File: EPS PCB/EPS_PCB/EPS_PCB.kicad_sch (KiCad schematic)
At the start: 0 parts

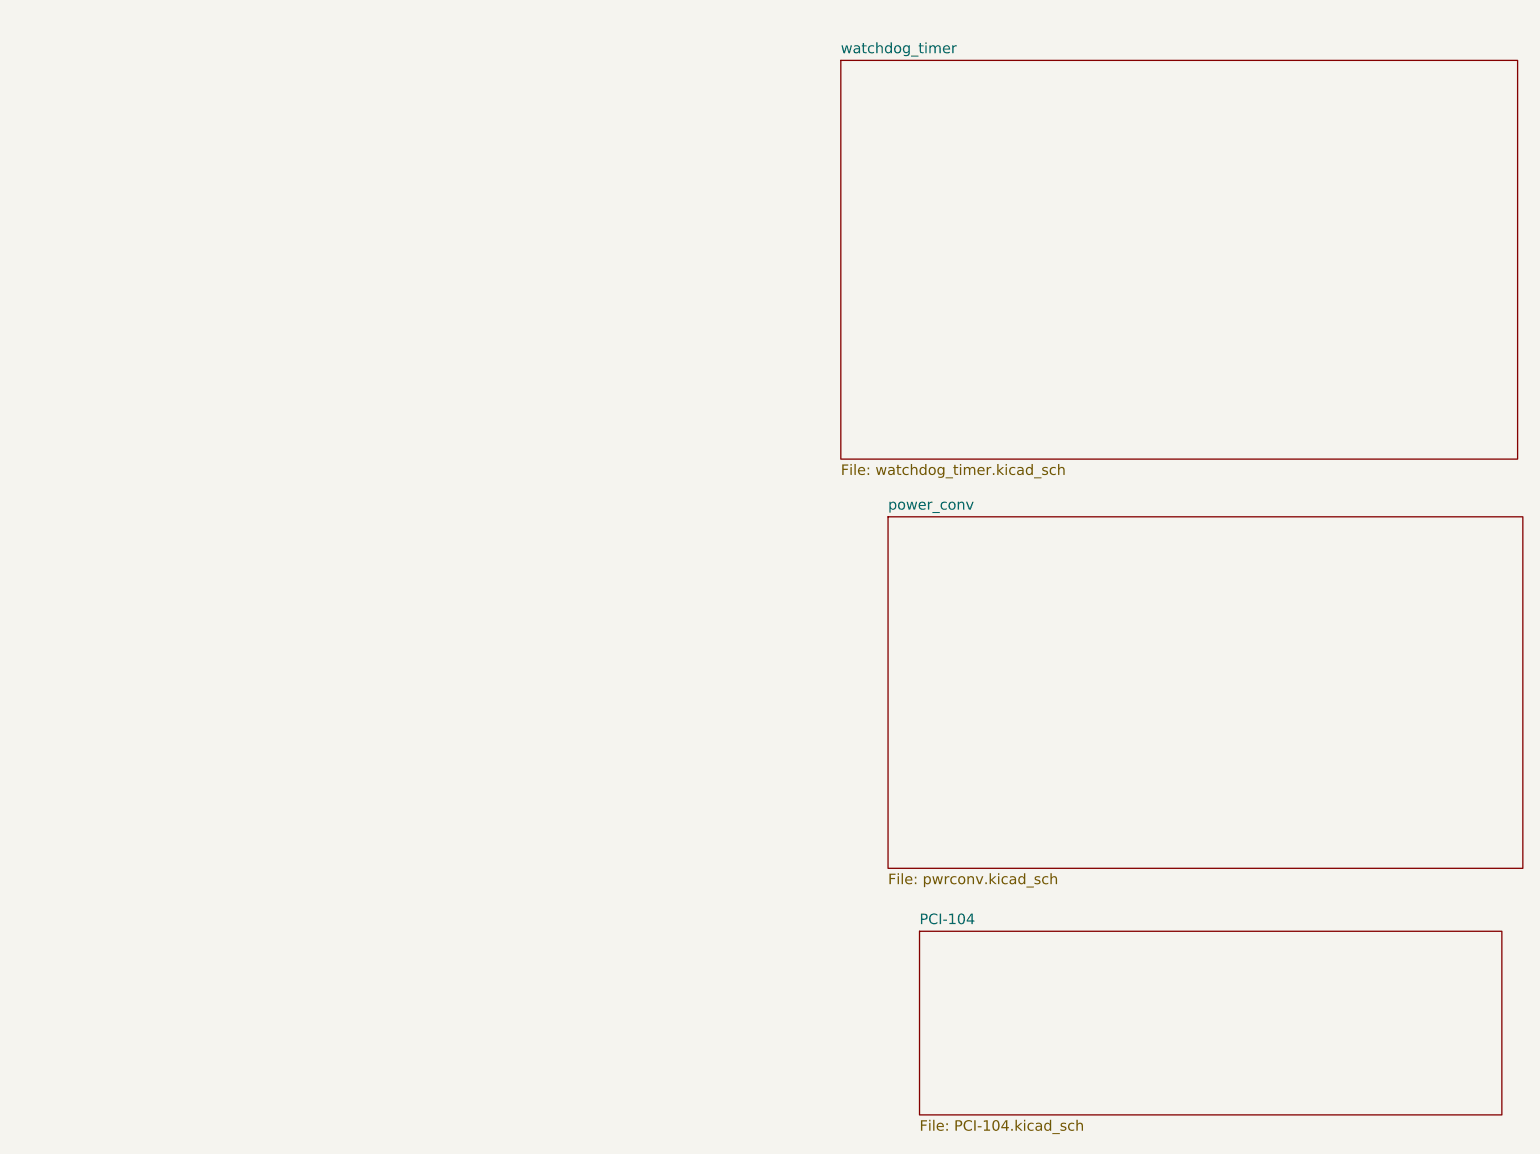
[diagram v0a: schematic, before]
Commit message: PDR Update
Added Current Measurement, Hysteresis, EFuses
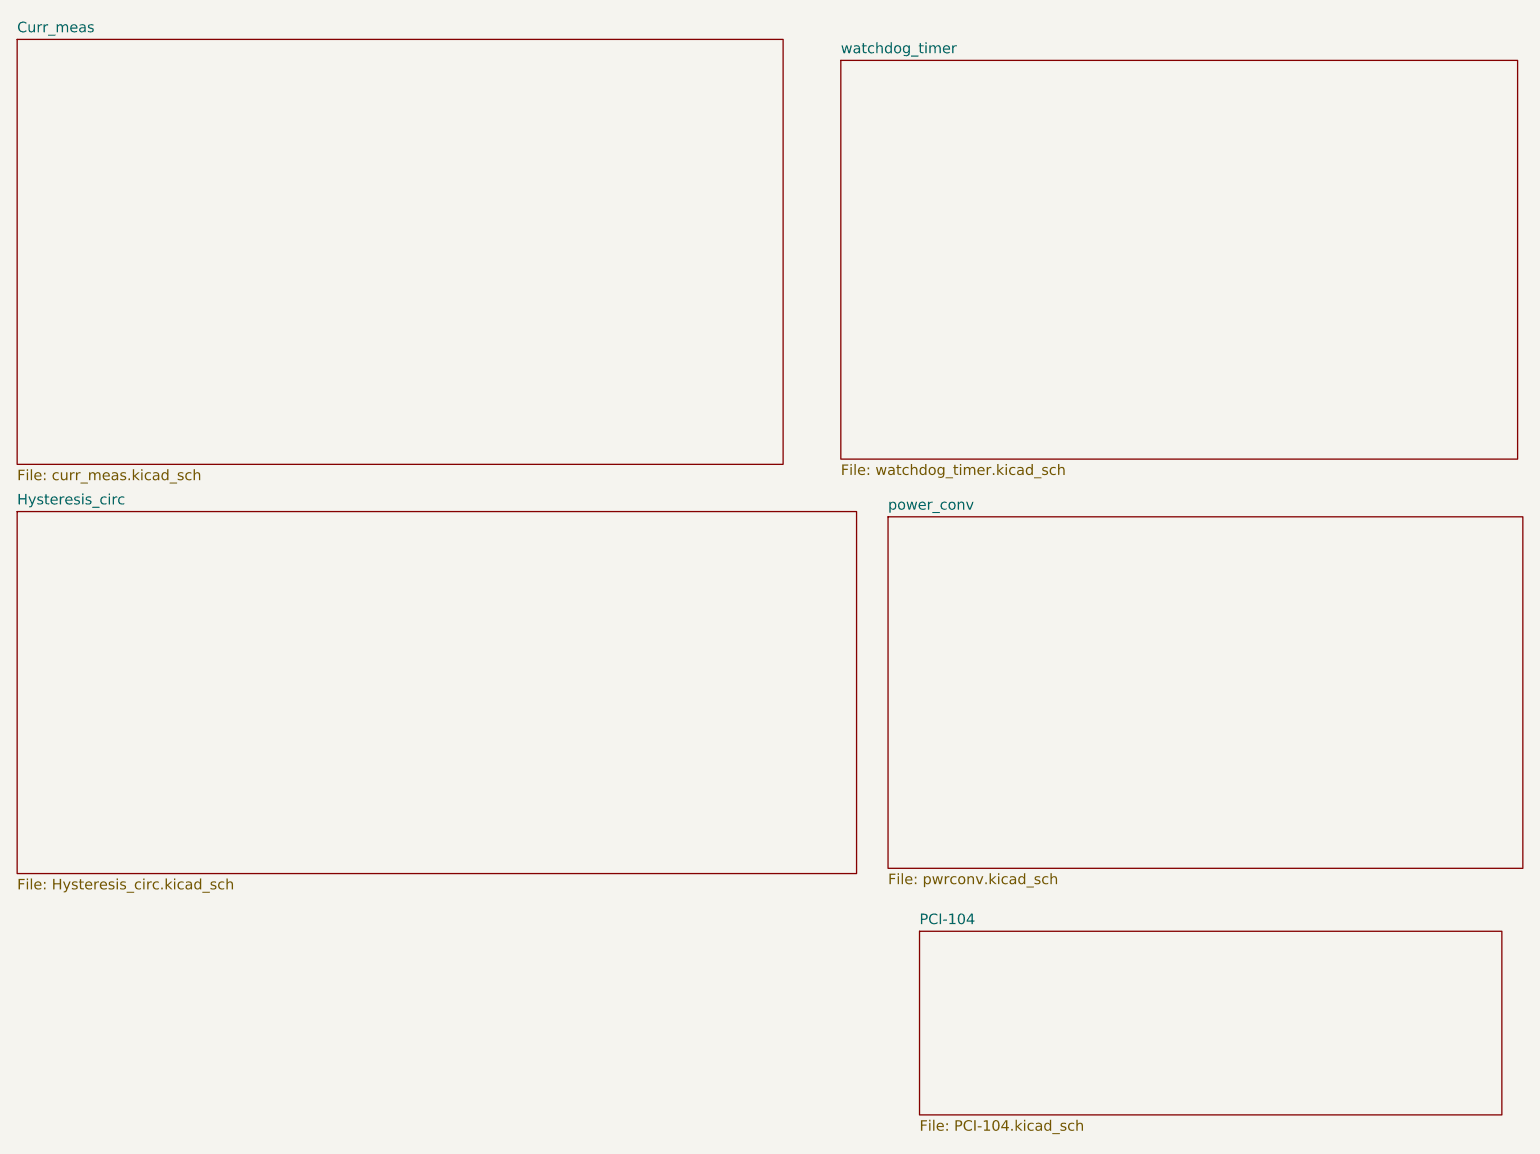
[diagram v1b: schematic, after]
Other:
- added sheet Curr_meas (curr_meas.kicad_sch)
- added sheet Hysteresis_circ (Hysteresis_circ.kicad_sch)
- company: (none) -> UW Huskysat
- title: (none) -> EPS_PDS_Circuit
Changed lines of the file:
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@@
 	(paper "A4")
 	(title_block
-		(date "2025-11-13")
+		(title "EPS_PDS_Circuit")
+		(date "2025-11-20")
+		(rev "1.0")
+		(company "UW Huskysat")
+		(comment 1 "Tracy, Maria, Phina, David, Chase")
 	)
 	(sheet
@@
 	)
 	(sheet
+		(at 90.805 27.305)
+		(size 92.71 51.435)
+		(exclude_from_sim no)
+		(in_bom yes)
+		(on_board yes)
+		(dnp no)
+		(fields_autoplaced yes)
+		(stroke
+			(width 0.1524)
+			(type solid)
+		)
+		(fill
+			(color 0 0 0 0.0000)
+		)
+		(property "Sheetname" "Curr_meas"
+			(at 90.805 26.5934 0)
+			(effects
+				(font
+					(size 1.27 1.27)
+				)
+				(justify left bottom)
+			)
+		)
+		(property "Sheetfile" "curr_meas.kicad_sch"
+			(at 90.805 79.3246 0)
+			(effects
+				(font
+					(size 1.27 1.27)
+				)
+				(justify left top)
+			)
+		)
+		(instances
+			(project "EPS_PCB"
+				(path "/e5aefcdf-1552-4881-b70a-fd78aade4bcb"
+					(page "5")
+				)
+			)
+		)
+	)
+	(sheet
 		(at 200.025 135.255)
 		(size 70.485 22.225)
@@
 				)
 			)
+		)
+	)
+	(sheet
+		(at 90.805 84.455)
+		(size 101.6 43.815)
+		(exclude_from_sim no)
+		(in_bom yes)
+		(on_board yes)
+		(dnp no)
+		(fields_autoplaced yes)
+		(stroke
+			(width 0.1524)
+			(type solid)
+		)
+		(fill
+			(color 0 0 0 0.0000)
+		)
+		(property "Sheetname" "Hysteresis_circ"
+			(at 90.805 83.7434 0)
+			(effects
+				(font
+					(size 1.27 1.27)
+				)
+				(justify left bottom)
+			)
+		)
+		(property "Sheetfile" "Hysteresis_circ.kicad_sch"
+			(at 90.805 128.8546 0)
+			(effects
+				(font
+					(size 1.27 1.27)
+				)
+				(justify left top)
+			)
+		)
+		(instances
+			(project "EPS_PCB"
+				(path "/e5aefcdf-1552-4881-b70a-fd78aade4bcb"
+					(page "6")
+				)
+			)
